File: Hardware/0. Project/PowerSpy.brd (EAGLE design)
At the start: 55 x 70.5 mm, 91 parts, among them IC1 CP2102N-A01-GQFN28, IC3 LM324D, P1 Mini-Fit 4T, T1 SS8050, T2 SS8050, U1 NCP1117ST33T3G, U2 HLK-PM01, U3 ADS1115IDGST, U4 ESP32-WROOM-32D, X1 4T PJ-321, X2 4T PJ-321, X3 USB Micro B

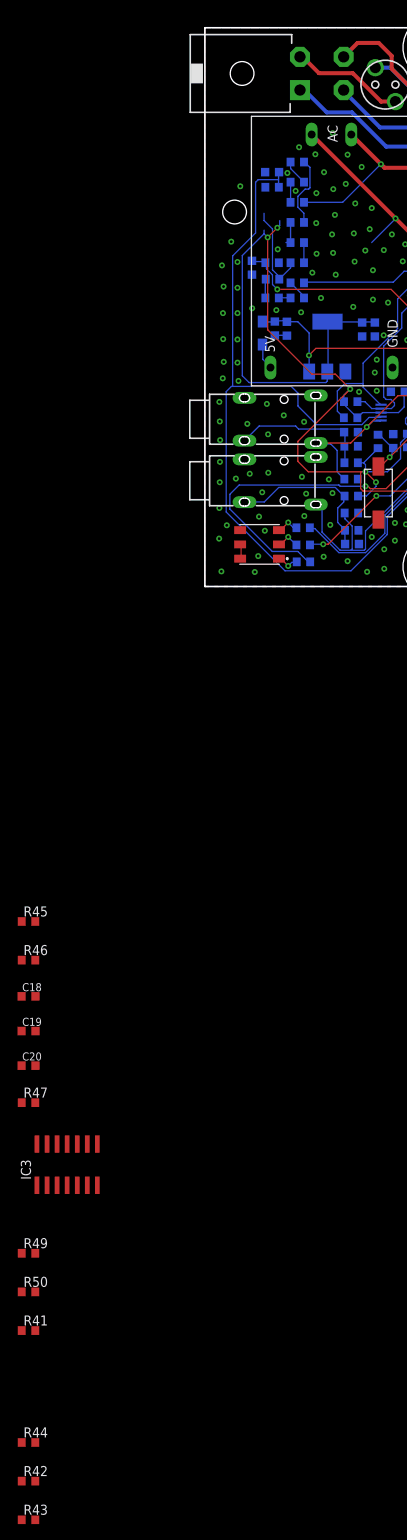
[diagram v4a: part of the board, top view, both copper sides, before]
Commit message: Schematic parts renumbered
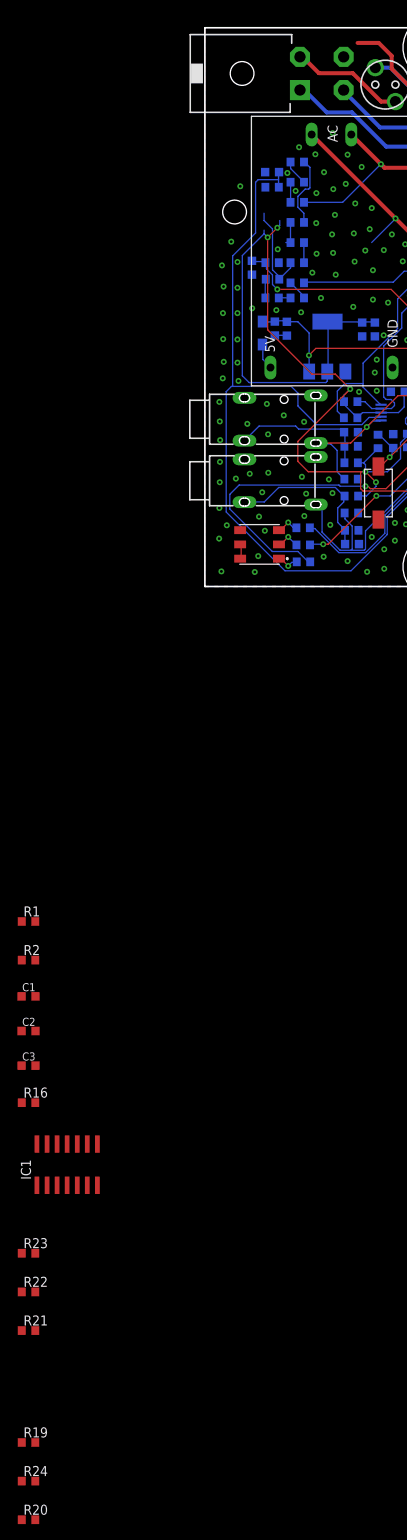
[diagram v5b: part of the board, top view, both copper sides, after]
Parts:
- removed C19: 100nF/50V (10%), rcl:C0603K
- removed C20: 10uF/10V (20%), rcl:C0603K
- removed D4: BAT760, diode:SOD323-W
- removed IC3: LM324D, linear:SO14
- removed R50: 100k (1%), rcl:R0603
- added C16, C17: 100nF/50V (10%), rcl:C0603K
- added D2: BAT760, diode:SOD323-W
- added IC2: CP2102N-A01-GQFN28, silabs:MLP28
- added R48: S05K130, varistor:S05K11
- C1, C14, C3: value 100nF/50V (10%) -> 10uF/10V (20%)
- C11: value 10nF/50V (10%) -> 100nF/50V (10%)
- C12: value 4.7uF/6.3V (10%) -> 100nF/50V (10%)
- C15: value 100nF/50V (10%) -> 10uF/6.3V (20%)
- C18: value 10uF/10V (20%) -> 10uF/6.3V (20%)
- C2: value 10uF/6.3V (20%) -> 100nF/50V (10%)
- C4: value 10uF/6.3V (20%) -> 10uF/10V (20%)
- C5: value 10uF/10V (20%) -> 4.7uF/6.3V (10%)
- C6: value 10uF/10V (20%) -> 100nF/50V (10%)
- C8: value 100nF/50V (10%) -> 10nF/50V (10%)
- F2: value SF70E -> 200 mA; device fuse:LITTLEFUSE -> fuse:QPL
- F5: value 200 mA -> SF70E; device fuse:QPL -> fuse:LITTLEFUSE
- IC1: value CP2102N-A01-GQFN28 -> LM324D; device silabs:MLP28 -> linear:SO14
- R1, R22: value 10k (5%) -> 100k (1%)
- R10: value S05K130 -> 100k (1%); device varistor:S05K11 -> rcl:R0603
- R11, R14: value 10k (1%) -> 100k (1%)
- R15, R23, R24: value 220k (1%) -> 100k (1%)
- R16: value 220k (1%) -> 220R (5%)
- R17, R18: value 100k (1%) -> 1k6 (1%)
- R19: value 47R (5%) -> 220R (5%)
- R2: value S05K230 -> 100k (1%); device varistor:S05K11 -> rcl:R0603
- R20: value 1k6 (1%) -> 100k (1%)
- R21: value 10k (5%) -> 220R (5%)
- R25, R42, R43: value 100k (1%) -> 10k (5%)
- R26: value 100k (1%) -> 47R (5%)
- R28: value 1k6 (1%) -> 1M (5%)
- R3: value S05K130 -> 22.1k (5%); device varistor:S05K11 -> rcl:R0603
- R30: value 10k (5%) -> 10k (5%)(NC)
- R31: value 10k (5%) -> 0R (5%)
- R32: value 10k (5%)(NC) -> 0R (5%)
- R33: value 22.1k (5%) -> 150R (5%)
- R34: value 10k (5%) -> 10k (1%)
- R35: value 0R (5%) -> 10k (1%)
- R36: value 0R (5%) -> 50R (5%)
- R37: value 47.5k (5%) -> 50R (5%)
- R39, R40: value 1M (5%) -> 10k (5%)
- R4: value 150R (5%) -> 47.5k (5%)
- R41: value 220R (5%) -> 10k (5%)
- R44: value 220R (5%) -> S05K230; device rcl:R0603 -> varistor:S05K11
- R45, R46, R49: value 100k (1%) -> S05K130; device rcl:R0603 -> varistor:S05K11
- R47: value 220R (5%) -> S05K130; device rcl:R0603 -> varistor:S05K11
- R5, R6: value 50R (5%) -> 220k (1%)
- R7: value S05K130 -> 1M (5%); device varistor:S05K11 -> rcl:R0603
- R8, R9: value S05K130 -> 220k (1%); device varistor:S05K11 -> rcl:R0603
- U1: value NCP1117ST33T3G -> ADS1115IDGST; device REG1117:SOT223 -> ADS1115IDGST:SOP50P490X110-10N
- U3: value ADS1115IDGST -> NCP1117ST33T3G; device ADS1115IDGST:SOP50P490X110-10N -> REG1117:SOT223
- X1: value 4T PJ-321 -> USB Micro B; device con-lumberg:1503_07 -> Micro USB Connector:ZX62D-B-5PA8
- X2: value 4T PJ-321 -> (none)
- X3: value USB Micro B -> (none); device Micro USB Connector:ZX62D-B-5PA8 -> con-lumberg:1503_07
- moved R44 175.7 mm to (38.0, 57.0), turned to 270 degrees
- moved R49 165.3 mm to (45.7, 66.6), turned to 90 degrees
- moved R20 164.7 mm to (-22.3, -117.8), flipped to the top, turned to 0 degrees
- moved R24 153.1 mm to (-22.3, -112.9), flipped to the top
- moved R19 152.0 mm to (-22.3, -108.0), flipped to the top, turned to 0 degrees
- moved R43 144.3 mm to (25.5, 18.4), flipped to the bottom, turned to 270 degrees
- moved R42 142.1 mm to (18.4, 23.3), flipped to the bottom, turned to 180 degrees
- moved R47 131.2 mm to (45.9, 47.0), turned to 90 degrees
- moved R23 127.0 mm to (-22.3, -84.1), flipped to the top
- moved R46 124.5 mm to (45.9, 57.0), turned to 270 degrees
- moved R45 124.4 mm to (38.0, 66.6), turned to 270 degrees
- moved R21 122.1 mm to (-22.3, -93.9), flipped to the top
- moved R41 122.1 mm to (18.4, 21.3), flipped to the bottom
- moved R16 121.0 mm to (-22.3, -65.1), flipped to the top, turned to 0 degrees
- moved R2 120.4 mm to (-22.3, -47.1), turned to 0 degrees
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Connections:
- removed net PE: P1.4, R10.2, R20.2, R28.2, R43.2, R47.1, R50.2, R8.2, R9.2
- net +4.1V: now also C3.1, IC1.4; no longer C20.1, IC3.4
- net 3.3V: now also C14.1, C16.1, C17.1, C18.1, C5.1, C6.1, IC2.6, IC2.7, R25.1, R34.1, R40.1, R41.1, R42.1, R43.1, U1.8, U3.2, U3.4; no longer C12.1, C13.1, C3.1, C4.1, C8.1, C9.1, IC1.6, IC1.7, R11.1, R21.1, R22.1, R30.1, R31.1, R45.1, U1.2, U1.4, U3.8
- net 5V: now also C13.1, C15.1, D2.C, U3.3; no longer C1.1, C2.1, D4.C, U1.3
- net ADC_ALERT: now also U1.2; no longer U3.2
- net ADC_CURRENT_L1: now also R7.1, U1.4, X2.1; no longer R39.1, U3.4, X1.1
- net ADC_CURRENT_L2: now also R28.1, U1.6, X3.1; no longer R40.1, U3.6, X2.1
- net ADC_SCL: now also R41.2, U1.10; no longer R21.2, U3.10
- net ADC_SDA: now also R42.2, U1.9; no longer R22.2, U3.9
- net ADC_VOLTAGE_L1: now also R26.1, U1.5; no longer R19.1, U3.5
- net ADC_VOLTAGE_L2: now also C8.1, U1.7; no longer C11.1, U3.7
- net BUTTON_PROG: now also R25.2; no longer R1.2
- net DTR: now also IC2.28, R38.2; no longer IC1.28, R34.2
- net EN: now also C12.1, R43.2; no longer C15.1, R31.2
- net GND: now also C16.2, C17.2, IC1.11, IC2.3, IC2.EXP, IC2.M, R2.2, R28.2, R30.1, R35.2, R4.1, R7.2, U1.3, X1.5; no longer C19.2, C20.2, IC1.3, IC1.EXP, IC1.M, IC3.11, R14.2, R32.1, R37.1, R39.2, R40.2, R46.2, U3.3, X3.5
- net IO0: now also C11.1, R40.2; no longer C14.1, R30.2
- net L1_VOLTAGE: now also F4.2, R44.1, R45.1, R49.1, R5.1; no longer F2.2, R10.1, R15.1, R2.1, R3.1
- net L2_VOLTAGE: now also F5.2, R44.2, R46.1, R48.1, R6.1; no longer F4.2, R2.2, R23.1, R7.1, R9.1
- net LED_BLUE: now also R37.1; no longer R6.1
- net LED_GREEN: now also R36.1; no longer R5.1
- net LED_RED: now also R33.1; no longer R4.1
- net N$1: now also IC2.11, R30.2; no longer IC1.11, R32.2
- net N$10: now also IC2.25, R32.2; no longer IC1.25, R36.2
- net N$11: now also C4.1, R12.2, X2.2@1; no longer C5.1, R11.2, X1.2@1
- net N$12: now also R10.1, R8.2; no longer R16.2, R17.1
- net N$13: now also IC1.1, IC1.2, R16.2; no longer IC3.1, IC3.2, R47.2
- net N$14: now also C1.1, C2.1, IC1.3, R1.2, R2.1; no longer C18.1, C19.1, IC3.3, R45.2, R46.1
- net N$15: now also IC1.7, R23.1, R26.2; no longer IC3.7, R19.2, R49.1
- net N$16: now also R15.2, R18.1, R19.2; no longer R26.2, R28.1, R44.2
- net N$17: now also F3.1; no longer F5.1
- net N$18: now also R10.2, R14.1; no longer R17.2, R18.1
- net N$19: now also R5.2, R8.1; no longer R15.2, R16.1
- net N$2: now also IC2.9; no longer IC1.9
- net N$20: now also IC1.8, R24.1; no longer IC3.8, R42.1
- net N$21: now also R36.2; no longer R5.2
- net N$22: now also C9.1, R34.2, R35.1, X3.2@1; no longer C6.1, R12.2, R14.1, X2.2@1
- net N$24: now also F2.2; no longer F3.2
- net N$25: now also F3.2; no longer F5.2
- net N$26: now also R37.2; no longer R6.2
- net N$27: now also R11.1, R9.2; no longer R24.2, R25.1
- net N$28: now also R11.2, R15.1; no longer R25.2, R26.1
- net N$29: now also R6.2, R9.1; no longer R23.2, R24.1
- net N$3: now also R33.2; no longer R4.2
- net N$30: now also IC1.6, R22.1, R23.2; no longer IC3.6, R49.2, R50.1
- net N$31: now also R14.2, R17.1, R21.2; no longer R18.2, R20.1, R41.2
- net N$32: now also IC1.5, R21.1; no longer IC3.5, R41.1
- net N$33: now also IC1.9, R20.1, R24.2; no longer IC3.9, R42.2, R43.1
- net N$34: now also IC1.10, R19.1; no longer IC3.10, R44.1
- net N$4: now also F4.1; no longer F2.1
- net N$5: now also R39.1; no longer R38.1
- net N$6: now also D2.A; no longer D1.A
- net N$7: now also R38.1; no longer R34.1
- net N$8: now also IC2.26, R31.2; no longer IC1.26, R35.2
- net N$9: now also F2.1, F5.1; no longer F3.1, F4.1
- net NEUTRAL: now also R16.1, R17.2, R18.2, R20.2, R22.2, R45.2, R46.2, R47.1, R47.2, R48.2, R49.2; no longer R3.2, R7.2, R8.1
- net RTS: now also IC2.24, R39.2; no longer IC1.24, R38.2
- net USB_CONNECTED: now also IC2.8, R3.1, R4.2; no longer IC1.8, R33.1, R37.2
- net USB_D+: now also IC2.4, X1.3; no longer IC1.4, X3.3
- net USB_D-: now also IC2.5, X1.2; no longer IC1.5, X3.2
- net USB_RX: now also R32.1; no longer R36.1
- net USB_TX: now also R31.1; no longer R35.1
- net VUSB: now also D1.A, R3.2, X1.1; no longer D4.A, R33.2, X3.1
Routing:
- net PE: track 73.1 -> 0.00 mm
- net NEUTRAL: track 79.5 -> 150.2 mm

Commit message: Another new and better AFE approach
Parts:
- removed IC1: LM324D, linear:SO14
- removed R10, R11: 100k (1%), rcl:R0603
- removed R13, R34, R35: 10k (1%), rcl:R0603
- removed R28, R7: 1M (5%), rcl:R0603
- added R50: 47R (5%), rcl:R0603
- added U5: MCP6024, MCP6024:14-SOIC
- added U6: MCP6021, MCP6024:SOT23-5
- C4, C9: value 10uF/10V (20%) -> 10nF/50V (10%)
- R12: value 10k (1%) -> 47R (5%)
- R14, R15: value 100k (1%) -> 200k (1%)
- R17, R18: value 1k6 (1%) -> 1k5 (1%)
- R27: value 47R (5%) -> 100R (5%)
- R5, R6, R8, R9: value 220k (1%) -> 200k (1%)
- X2, X3: value (none) -> Jack J2 Stereo
- moved C9 199.3 mm to (-30.6, -173.7), flipped to the top, turned to 0 degrees
- moved C4 162.8 mm to (-30.6, -149.9), flipped to the top, turned to 0 degrees
- moved R12 161.6 mm to (-20.9, -145.3), flipped to the top
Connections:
- removed net N$28: R11.2, R15.1
- new net N$35: U5.10, X2.1
- new net N$36: U5.12, X3.1
- new net PE: X2.2@1
- net +4.1V: now also U5.4, U6.5; no longer IC1.4
- net 3.3V: no longer R12.1, R34.1
- net ADC_CURRENT_L1: now also C4.1, R12.1; no longer R7.1, X2.1
- net ADC_CURRENT_L2: now also C9.1, R50.1; no longer R28.1, X3.1
- net GND: now also U5.11, U6.2; no longer IC1.11, R13.2, R28.2, R35.2, R7.2
- net N$11: now also U5.8, U5.9; no longer C4.1, R13.1, X2.2@1
- net N$12: now also R14.1; no longer R10.1
- net N$13: now also U6.1, U6.4; no longer IC1.1, IC1.2
- net N$14: now also U6.3; no longer IC1.3
- net N$15: now also U5.1; no longer IC1.7
- net N$18: now also P1.4, R47.2, R48.2, R49.2; no longer R10.2, R14.1
- net N$20: now also U5.7; no longer IC1.8
- net N$22: now also R50.2, U5.13, U5.14; no longer C9.1, R34.2, R35.1, X3.2@1
- net N$27: now also R15.1; no longer R11.1
- net N$30: now also U5.2; no longer IC1.6
- net N$32: now also U5.3; no longer IC1.5
- net N$33: now also U5.6; no longer IC1.9
- net N$34: now also U5.5; no longer IC1.10
- net NEUTRAL: now also X3.2@1; no longer R47.2, R48.2, R49.2
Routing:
- net NEUTRAL: track 150.2 -> 81.9 mm
- net N$11: track 20.6 -> 0.00 mm
- net N$22: track 17.7 -> 0.00 mm
- net ADC_CURRENT_L2: track 37.7 -> 26.3 mm
- net N$18: track 9.18 -> 0.00 mm
- net N$12: track 3.24 -> 12.2 mm
- net N$28: track 2.40 -> 0.00 mm
- net N$27: track 1.48 -> 3.74 mm
- net ADC_CURRENT_L1: track 55.5 -> 54.6 mm
- net 3.3V: track 206.1 -> 205.3 mm

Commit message: Schematic parts renumbered
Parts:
- removed R44: S05K230, varistor:S05K11
- removed R45, R46, R47, R48, R49: S05K130, varistor:S05K11
- added R10, R11, R7: 200k (1%), rcl:R0603
- added R13: 1k5 (1%), rcl:R0603
- added R34, R35: 10k (5%), rcl:R0603
- C4: value 10nF/50V (10%) -> 4.7uF/6.3V (10%)
- C5: value 4.7uF/6.3V (10%) -> 10nF/50V (10%)
- R12: value 47R (5%) -> 1k5 (1%)
- R14, R15: value 200k (1%) -> 220R (5%)
- R16, R19: value 220R (5%) -> 100k (1%)
- R17: value 1k5 (1%) -> 220R (5%)
- R18: value 1k5 (1%) -> 100k (1%)
- R21: value 220R (5%) -> 10k (5%)
- R22: value 100k (1%) -> 100R (5%)
- R23: value 100k (1%) -> 47R (5%)
- R24: value 100k (1%) -> 2k (5%)
- R25: value 10k (5%) -> 10k (5%)(NC)
- R26: value 47R (5%) -> 0R (5%)
- R27: value 100R (5%) -> 0R (5%)
- R29: value 2k (5%) -> 150R (5%)
- R30: value 10k (5%)(NC) -> 50R (5%)
- R31: value 0R (5%) -> 10k (5%)
- R32: value 0R (5%) -> 50R (5%)
- R33: value 150R (5%) -> 10k (5%)
- R36, R37: value 50R (5%) -> 10k (5%)
- R38: value 10k (5%) -> S05K230; device rcl:R0603 -> varistor:S05K11
- R39, R40, R41, R42, R43: value 10k (5%) -> S05K130; device rcl:R0603 -> varistor:S05K11
- R9: value 200k (1%) -> 47R (5%)
- U1: value ADS1115IDGST -> MCP6021; device ADS1115IDGST:SOP50P490X110-10N -> MCP6024:SOT23-5
- U2: value HLK-PM01 -> MCP6024; device HLK-PM01:HLK-PM01 -> MCP6024:14-SOIC
- U3: value NCP1117ST33T3G -> ADS1115IDGST; device REG1117:SOT223 -> ADS1115IDGST:SOP50P490X110-10N
- U4: value ESP32-WROOM-32D -> HLK-PM01; device ESP32-WROOM-32D:MODULE_ESP32-WROOM-32D -> HLK-PM01:HLK-PM01
- U5: value MCP6024 -> NCP1117ST33T3G; device MCP6024:14-SOIC -> REG1117:SOT223
- U6: value MCP6021 -> ESP32-WROOM-32D; device MCP6024:SOT23-5 -> ESP32-WROOM-32D:MODULE_ESP32-WROOM-32D
- moved U6 217.2 mm to (42.8, 29.0), flipped to the bottom, turned to 90 degrees
- moved U1 204.6 mm to (-34.1, -174.1), flipped to the top
- moved R12 189.0 mm to (11.7, 40.9), flipped to the bottom, turned to 180 degrees
- moved R9 184.6 mm to (-20.9, -145.3), flipped to the top
- moved C4 172.5 mm to (45.4, 4.98), flipped to the bottom, turned to 180 degrees
- moved C5 172.5 mm to (-30.6, -149.9), flipped to the top, turned to 0 degrees
- moved U2 162.1 mm to (-27.5, -113.8), turned to 0 degrees
- moved U5 150.3 mm to (15.5, 30.3), flipped to the bottom
- moved R15 150.0 mm to (-22.3, -108.0), flipped to the top, turned to 0 degrees
- moved R22 142.7 mm to (8.48, 50.4), flipped to the bottom
- moved R17 141.4 mm to (-22.3, -93.9), flipped to the top, turned to 0 degrees
- moved R18 134.2 mm to (-22.3, -89.0), flipped to the top, turned to 0 degrees
- moved R24 131.5 mm to (40.7, 2.54), flipped to the bottom, turned to 270 degrees
- moved R23 128.7 mm to (8.48, 40.9), flipped to the bottom, turned to 180 degrees
- moved R21 122.3 mm to (32.2, 15.7), flipped to the bottom, turned to 270 degrees
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- renumbered IC2 to IC1, P1 to CN1, R50 to R28
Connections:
- net +4.1V: now also U1.5, U2.4; no longer U5.4, U6.5
- net 3.3V: now also C4.1, R21.1, R24.2, R34.1, R35.1, R36.1, R37.1, U3.8, U5.2, U5.4, U6.2; no longer C5.1, R25.1, R29.2, R40.1, R41.1, R42.1, R43.1, U1.8, U3.2, U3.4, U4.2
- net 5V: now also U5.3; no longer U3.3
- net ADC_ALERT: now also U3.2, U6.31; no longer U1.2, U4.31
- net ADC_CURRENT_L1: now also C5.1, R9.1, U3.4, U6.8; no longer C4.1, R12.1, U1.4, U4.8
- net ADC_CURRENT_L2: now also U3.6, U6.9; no longer U1.6, U4.9
- net ADC_SCL: now also R35.2, U3.10, U6.36; no longer R41.2, U1.10, U4.36
- net ADC_SDA: now also R37.2, U3.9, U6.33; no longer R42.2, U1.9, U4.33
- net ADC_VOLTAGE_L1: now also R23.1, U3.5, U6.6; no longer R26.1, U1.5, U4.6
- net ADC_VOLTAGE_L2: now also R22.1, U3.7, U6.7; no longer R27.1, U1.7, U4.7
- net BUTTON_PROG: now also R21.2, U6.37; no longer R25.2, U4.37
- net DTR: now also R31.2; no longer R38.2
- net EN: now also R36.2, U6.3; no longer R43.2, U4.3
- net GND: now also R25.1, U1.2, U2.11, U3.3, U4.P$3, U5.1, U6.1, U6.15, U6.38, U6.39; no longer R30.1, U1.1, U1.3, U2.P$3, U4.1, U4.15, U4.38, U4.39, U5.11, U6.2
- net IO0: now also R34.2, U6.25; no longer R40.2, U4.25
- net L1_VOLTAGE: now also R38.1, R39.1, R43.1, R6.1, U4.P$1; no longer R44.1, R45.1, R49.1, R5.1, U2.P$1
- net L2_VOLTAGE: now also R38.2, R40.1, R42.1, R5.1; no longer R44.2, R46.1, R48.1, R6.1
- net LED_BLUE: now also R32.1, U6.12; no longer R37.1, U4.12
- net LED_GREEN: now also R30.1, U6.11; no longer R36.1, U4.11
- net LED_RED: now also R29.1, U6.10; no longer R33.1, U4.10
- net N$1: now also R25.2; no longer R30.2
- net N$10: now also R27.2; no longer R32.2
- net N$11: now also R9.2, U2.8, U2.9; no longer R12.2, U5.8, U5.9
- net N$12: now also R11.1; no longer R14.1
- net N$13: now also R14.2, U1.1, U1.4; no longer R16.2, U6.1, U6.4
- net N$14: now also U1.3; no longer U6.3
- net N$15: now also R19.1, R23.2, U2.1; no longer R23.1, R26.2, U5.1
- net N$16: now also R10.2, R12.1; no longer R18.1, R19.2
- net N$18: now also R41.2, R42.2, R43.2; no longer R47.2, R48.2, R49.2
- net N$19: now also R6.2; no longer R5.2
- net N$2: now also R24.1; no longer R29.1
- net N$20: now also R20.1, R22.2, U2.7; no longer R24.1, R27.2, U5.7
- net N$21: now also R30.2; no longer R36.2
- net N$22: now also U2.13, U2.14; no longer U5.13, U5.14
- net N$26: now also R32.2; no longer R37.2
- net N$27: now also R10.1, R7.2; no longer R15.1, R9.2
- net N$29: now also R5.2, R7.1; no longer R6.2, R9.1
- net N$3: now also R29.2; no longer R33.2
- net N$30: now also R18.1, R19.2, U2.2; no longer R22.1, R23.2, U5.2
- net N$31: now also R11.2, R13.1, R17.2; no longer R14.2, R17.1, R21.2
- net N$32: now also R17.1, U2.3; no longer R21.1, U5.3
- net N$33: now also R16.1, R20.2, U2.6; no longer R20.1, R24.2, U5.6
- net N$34: now also R15.1, U2.5; no longer R19.1, U5.5
- net N$35: now also U2.10; no longer U5.10
- net N$36: now also U2.12; no longer U5.12
- net N$5: now also R33.1; no longer R39.1
- net N$6: now also U4.P$4; no longer U2.P$4
- net N$7: now also R31.1; no longer R38.1
- net N$8: now also R26.2; no longer R31.2
- net NEUTRAL: now also R12.2, R13.2, R14.1, R16.2, R39.2, R40.2, R41.1, U4.P$2; no longer R16.1, R17.2, R20.2, R22.2, R45.2, R46.2, R47.1, U2.P$2
- net RTS: now also R33.2; no longer R39.2
- net USB_RX: now also R27.1, U6.35; no longer R32.1, U4.35
- net USB_TX: now also R26.1, U6.34; no longer R31.1, U4.34

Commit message: Minor improvements
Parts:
- added C19: 100nF/50V (10%), rcl:C0603K
- C3: value 10uF/10V (20%) -> 100nF/50V (10%)
- moved C3 118.3 mm to (-34.5, -178.1)
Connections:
- net +4.1V: now also C19.1
- net GND: now also C19.2
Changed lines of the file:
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@@
 <attribute name="VALUE" x="-23.0504" y="-57.7332" size="1.016" layer="27"/>
-</element>
-<element name="C3" library="rcl" library_urn="urn:adsk.eagle:library:334" package="C0603K" package3d_urn="urn:adsk.eagle:package:23680/2" value="10uF/10V (20%)" x="-22.2504" y="-60.452" smashed="yes">
-<attribute name="NAME" x="-23.0504" y="-59.802" size="1.016" layer="25"/>
-<attribute name="POPULARITY" value="30" x="-22.2504" y="-60.452" size="1.778" layer="27" display="off"/>
-<attribute name="SPICEPREFIX" value="C" x="-22.2504" y="-60.452" size="1.778" layer="27" display="off"/>
-<attribute name="VALUE" x="-23.0504" y="-62.102" size="1.016" layer="27"/>
 </element>
 <element name="R14" library="rcl" library_urn="urn:adsk.eagle:library:334" package="R0603" package3d_urn="urn:adsk.eagle:package:23555/3" value="220R (5%)" x="-22.2504" y="-65.1256" smashed="yes">
@@
 </element>
 <element name="U1" library="MCP6024" package="SOT23-5" value="MCP6021" x="-34.1376" y="-174.1424" smashed="yes"/>
+<element name="C3" library="rcl" library_urn="urn:adsk.eagle:library:334" package="C0603K" package3d_urn="urn:adsk.eagle:package:23680/2" value="100nF/50V (10%)" x="-34.544" y="-178.1048" smashed="yes">
+<attribute name="NAME" x="-35.344" y="-177.4548" size="1.016" layer="25"/>
+<attribute name="POPULARITY" value="30" x="-34.544" y="-178.1048" size="1.778" layer="27" display="off"/>
+<attribute name="SPICEPREFIX" value="C" x="-34.544" y="-178.1048" size="1.778" layer="27" display="off"/>
+<attribute name="VALUE" x="-35.344" y="-179.7548" size="1.016" layer="27"/>
+</element>
+<element name="C19" library="rcl" library_urn="urn:adsk.eagle:library:334" package="C0603K" package3d_urn="urn:adsk.eagle:package:23680/2" value="100nF/50V (10%)" x="-34.544" y="-182.4736" smashed="yes">
+<attribute name="NAME" x="-35.344" y="-181.8236" size="1.016" layer="25"/>
+<attribute name="POPULARITY" value="30" x="-34.544" y="-182.4736" size="1.778" layer="27" display="off"/>
+<attribute name="SPICEPREFIX" value="C" x="-34.544" y="-182.4736" size="1.778" layer="27" display="off"/>
+<attribute name="VALUE" x="-35.344" y="-184.1236" size="1.016" layer="27"/>
+</element>
 </elements>
 <signals>
@@
 <contactref element="C1" pad="2"/>
 <contactref element="C2" pad="2"/>
-<contactref element="C3" pad="2"/>
 <contactref element="C5" pad="2"/>
 <contactref element="C9" pad="2"/>
 <contactref element="U2" pad="11"/>
 <contactref element="U1" pad="2"/>
+<contactref element="C3" pad="2"/>
+<contactref element="C19" pad="2"/>
+<wire x1="-33.669" y1="-178.1048" x2="-33.669" y2="-182.4736" width="0" layer="19" extent="1-1"/>
+<wire x1="-35.3314" y1="-174.1424" x2="-33.669" y2="-178.1048" width="0" layer="19" extent="1-1"/>
 <wire x1="-29.7066" y1="-173.736" x2="-35.3314" y2="-174.1424" width="0" layer="19" extent="1-1"/>
 <wire x1="-29.7066" y1="-149.86" x2="-29.7066" y2="-173.736" width="0" layer="19" extent="1-1"/>
 <wire x1="-25.0786" y1="-113.792" x2="-29.7066" y2="-149.86" width="0" layer="19" extent="1-1"/>
-<wire x1="-21.3754" y1="-60.452" x2="-25.0786" y2="-113.792" width="0" layer="19" extent="1-1"/>
-<wire x1="-21.3754" y1="-56.0832" x2="-21.3754" y2="-60.452" width="0" layer="19" extent="1-1"/>
+<wire x1="-21.3754" y1="-56.0832" x2="-25.0786" y2="-113.792" width="0" layer="19" extent="1-1"/>
 <wire x1="-21.3754" y1="-51.7144" x2="-21.3754" y2="-56.0832" width="0" layer="19" extent="1-1"/>
 <wire x1="-21.4004" y1="-47.1424" x2="-21.3754" y2="-51.7144" width="0" layer="19" extent="1-1"/>
@@
 </signal>
 <signal name="+4.1V">
-<contactref element="C3" pad="1"/>
 <contactref element="U2" pad="4"/>
 <contactref element="U1" pad="5"/>
+<contactref element="C3" pad="1"/>
+<contactref element="C19" pad="1"/>
+<wire x1="-35.419" y1="-178.1048" x2="-35.419" y2="-182.4736" width="0" layer="19" extent="1-1"/>
+<wire x1="-32.9438" y1="-173.1924" x2="-35.419" y2="-178.1048" width="0" layer="19" extent="1-1"/>
 <wire x1="-29.9886" y1="-113.792" x2="-32.9438" y2="-173.1924" width="0" layer="19" extent="1-1"/>
-<wire x1="-23.1254" y1="-60.452" x2="-29.9886" y2="-113.792" width="0" layer="19" extent="1-1"/>
 </signal>
 <signal name="N$14">
